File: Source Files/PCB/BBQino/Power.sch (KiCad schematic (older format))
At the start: 14 parts, among them J1 VIN < 13V, Q1 IPD068P03L3G, U1 ADP7142ARDZ-5.0

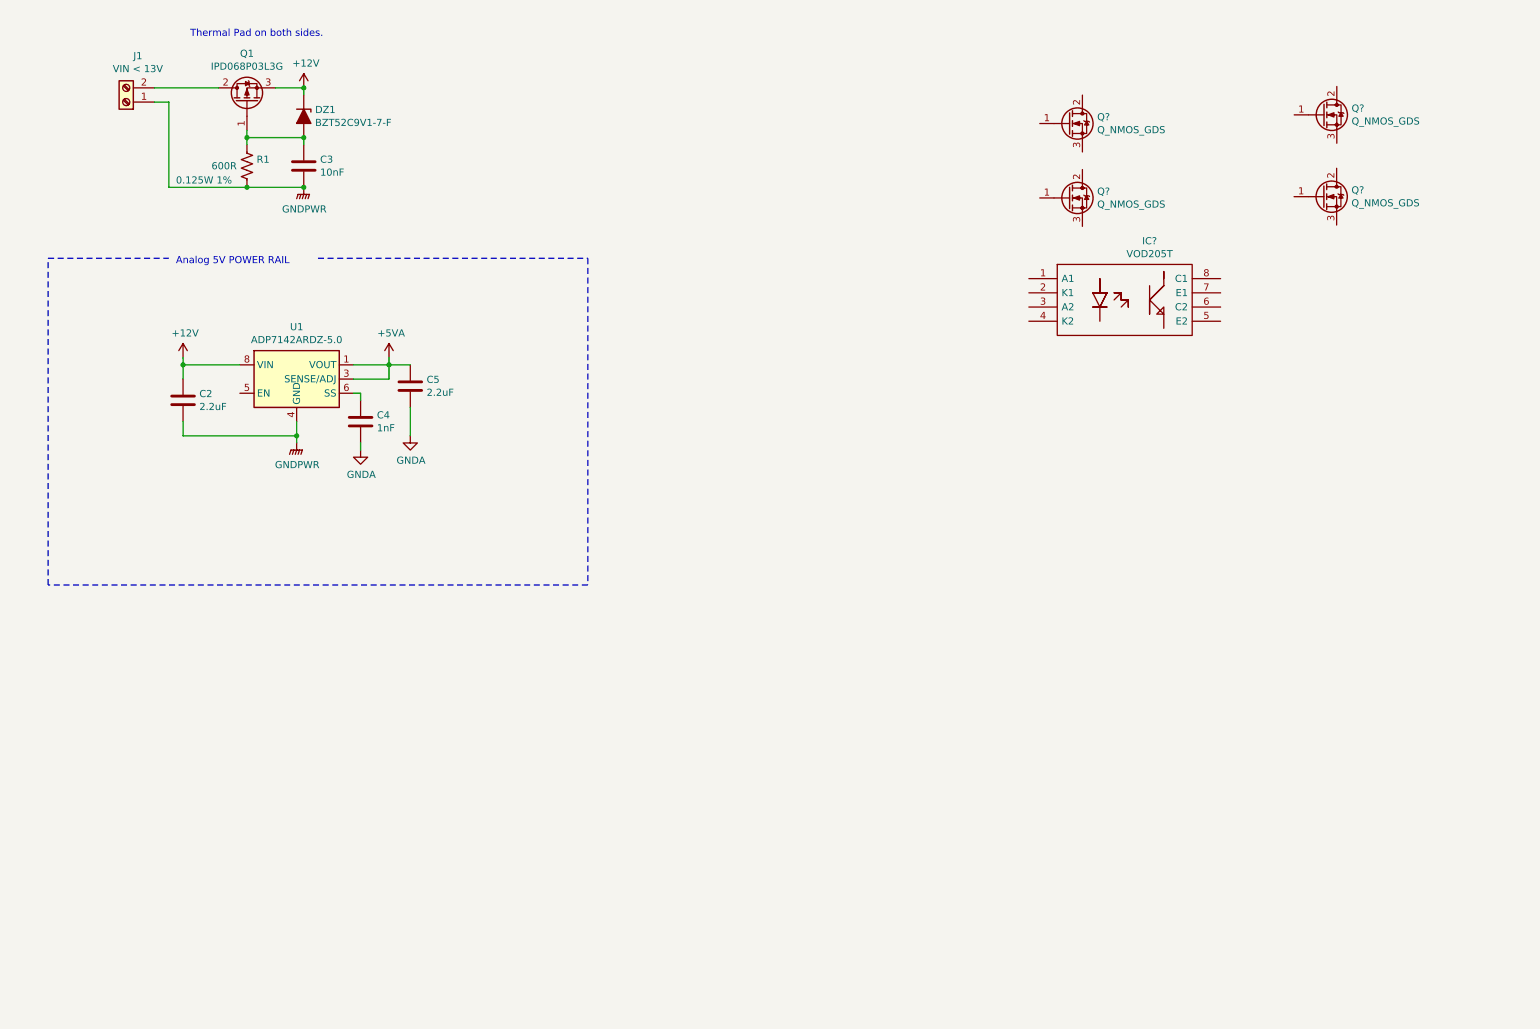
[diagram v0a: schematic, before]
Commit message: added current sense on motor side
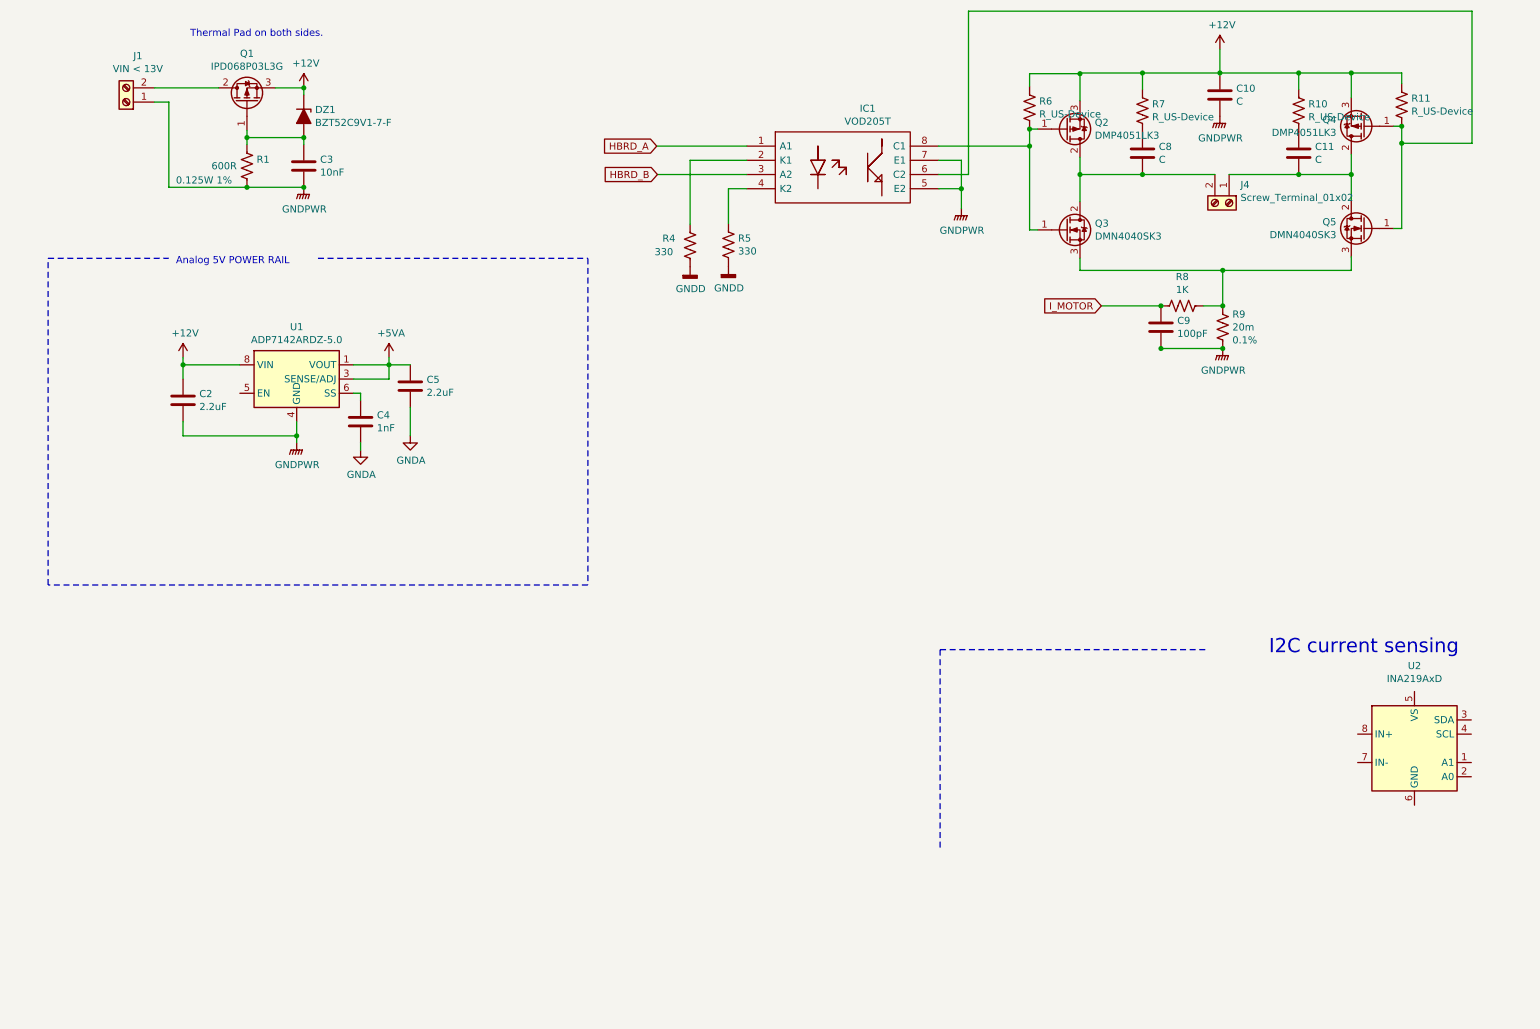
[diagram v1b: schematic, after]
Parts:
- removed Q? (x4): Q_NMOS_GDS, symbol Device:Q_NMOS_GDS
- added C10, C11, C8: C, symbol Device:C
- added C9: 100pF, symbol Device:C
- added J4: Screw_Terminal_01x02, symbol Connector:Screw_Terminal_01x02
- added Q2, Q4: DMP4051LK3, Package_TO_SOT_SMD:TO-252-3_TabPin2, symbol Device:Q_PMOS_GDS
- added Q3, Q5: DMN4040SK3, Package_TO_SOT_SMD:TO-252-3_TabPin2, symbol Device:Q_NMOS_GDS
- added R10, R11, R6, R7: R_US-Device, symbol BBQino-rescue:R_US-Device
- added R4, R5: 330, Resistor_SMD:R_0805_2012Metric_Pad1.20x1.40mm_HandSolder, symbol BBQino-rescue:R_US-Device
- added R8: 1K, symbol BBQino-rescue:R_US-Device
- added R9: 20m, symbol BBQino-rescue:R_US-Device
- added U2: INA219AxD, Package_SO:SOIC-8_3.9x4.9mm_P1.27mm, symbol Analog_ADC:INA219AxD
- gave numbers to parts that had none: 1
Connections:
- net +12V: now also Q2.3 (S), Q4.3 (S), R10.1, R11.1, R6.1, R7.1
- net GNDPWR: now also IC1.5 (E2), IC1.7 (E1), C10.2, C9.2, R9.2
- net HBRD_A: now reaches IC1.1 (A1)
- net at IC1.2 (K1): now also R4.1
- net HBRD_B: now reaches IC1.3 (A2)
- net at IC1.4 (K2): now also R5.1
- net at IC1.6 (C2): now also Q4.1 (G), Q5.1 (G), R11.2
- net at IC1.8 (C1): now also Q2.1 (G), Q3.1 (G), R6.2
- new net: C8.2, J4.2 (Pin_2), Q2.2 (D), Q3.2 (D)
- new net: Q3.3 (S), Q5.3 (S), R8.1, R9.1
- new net: C11.2, J4.1 (Pin_1), Q4.2 (D), Q5.2 (D)
- new net: C8.1, R7.2
- new net: C11.1, R10.2
- new net GNDD: R4.2, R5.2
- new net I_MOTOR: C9.1, R8.2
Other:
- note added: "I2C current sensing\n"
- moved on the sheet: IC1

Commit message: updated schematic
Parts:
- added C?: C, symbol Device:C
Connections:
- wire segments 83 -> 90
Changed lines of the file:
@@
 $EndComp
 Wire Wire Line
-	9015 1760 9505 1760
-Wire Wire Line
-	8915 1760 8405 1760
+	9015 1760 9206 1760
+Wire Wire Line
+	8915 1760 8702 1760
 $Comp
 L Device:C C8
@@
 Wire Notes Line
 	6980 5105 6980 6500
+$Comp
+L Device:C C?
+U 1 1 619C74D7
+P 8968 1620
+F 0 "C?" H 9083 1666 50  0000 L CNN
+F 1 "C" H 9083 1575 50  0000 L CNN
+F 2 "" H 9006 1470 50  0001 C CNN
+F 3 "~" H 8968 1620 50  0001 C CNN
+	1    8968 1620
+	0    1    1    0
+$EndComp
+Wire Wire Line
+	9118 1620 9206 1620
+Wire Wire Line
+	9206 1620 9206 1760
+Connection ~ 9206 1760
+Wire Wire Line
+	9206 1760 9505 1760
+Wire Wire Line
+	8820 1620 8818 1620
+Wire Wire Line
+	8702 1620 8702 1760
+Connection ~ 8818 1620
+Wire Wire Line
+	8818 1620 8702 1620
+Connection ~ 8702 1760
+Wire Wire Line
+	8702 1760 8405 1760
 $EndSCHEMATC

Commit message: New architecture
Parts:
- removed C10, C11, C8, C?: C, symbol Device:C
- removed C9: 100pF, symbol Device:C
- removed IC1: VOD205T, SOIC127P610X323-8N, symbol BBQino-rescue:VOD205T
- removed J4: Screw_Terminal_01x02, symbol Connector:Screw_Terminal_01x02
- removed Q2, Q4: DMP4051LK3, Package_TO_SOT_SMD:TO-252-3_TabPin2, symbol Device:Q_PMOS_GDS
- removed Q3, Q5: DMN4040SK3, Package_TO_SOT_SMD:TO-252-3_TabPin2, symbol Device:Q_NMOS_GDS
- removed U2: INA219AxD, Package_SO:SOIC-8_3.9x4.9mm_P1.27mm, symbol Analog_ADC:INA219AxD
- added C10, C11, C12, C19, C20, C21: 1uF, Capacitor_SMD:C_0805_2012Metric_Pad1.18x1.45mm_HandSolder, symbol BBQino-rescue:C-Device
- added C8, C9: 2.2nF, Capacitor_SMD:C_0805_2012Metric_Pad1.18x1.45mm_HandSolder, symbol BBQino-rescue:C-Device
- added D14, D15: BAS316, Diode_SMD:D_SOD-323, symbol Diode:BAS316
- added D16, D17: B140-E3, Diode_SMD:D_SMA, symbol Diode:B140-E3
- added D18, D19: BZM55Bxx, Diode_SMD:D_MicroMELF, symbol Diode:BZM55Bxx
- added D9: SD36_SOD323, Diode_SMD:D_SOD-323, symbol Diode:SD36_SOD323
- added Q12, Q13: BC846BPN, Package_TO_SOT_SMD:SOT-363_SC-70-6, symbol Transistor_BJT:BC846BPN
- added Q2, Q3, Q4, Q5: BC846, Package_TO_SOT_SMD:SOT-23, symbol Transistor_BJT:BC846
- added R14: 2.2k, symbol BBQino-rescue:R_US-Device
- added R15, R16, R17, R32, R33: 10k, symbol BBQino-rescue:R_US-Device
- added R30, R31: 1k, symbol BBQino-rescue:R_US-Device
- added U2: LM358, symbol Amplifier_Operational:LM358
- added U4: 74LVC2G14, symbol 74xGxx:74LVC2G14
- R10, R11: value R_US-Device -> 1k
- R4, R5: value 330 -> 10k; footprint Resistor_SMD:R_0805_2012Metric_Pad1.20x1.40mm_HandSolder -> (none); Value2 (none) -> 1%
- R6: value R_US-Device -> 2.2k; Value2 (none) -> 1%
- R7: value R_US-Device -> 10k; Value2 (none) -> 1%
- R8: value 1K -> 4.7k
- R9: value 20m -> 4.7k; Value2 0.1% -> (none)
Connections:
- net labels added: HS_G_L, HS_G_R, PWM_A, PWM_L_HS, PWM_L_LS, PWM_R_HS, float_1, float_2
- net labels removed: HBRD_A, HBRD_B, I_MOTOR
- wire segments 90 -> 167
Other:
- note added: "BOOTSTRAP\n"
- note added: "DEAD TIME\n"
- note added: "UNUSED PARTS"
- note added: "\PWM_L_HS\n"
- note removed: "I2C current sensing\n"
- moved on the sheet: J1
